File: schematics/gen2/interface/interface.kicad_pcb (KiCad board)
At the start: 2 copper layers, 100 x 91 mm, 17 parts, among them U1 74LS00, U2 74LS00, U4 74LS245, U5 74LS193, U6 74LS193, U7 74LS193, U8 74LS193

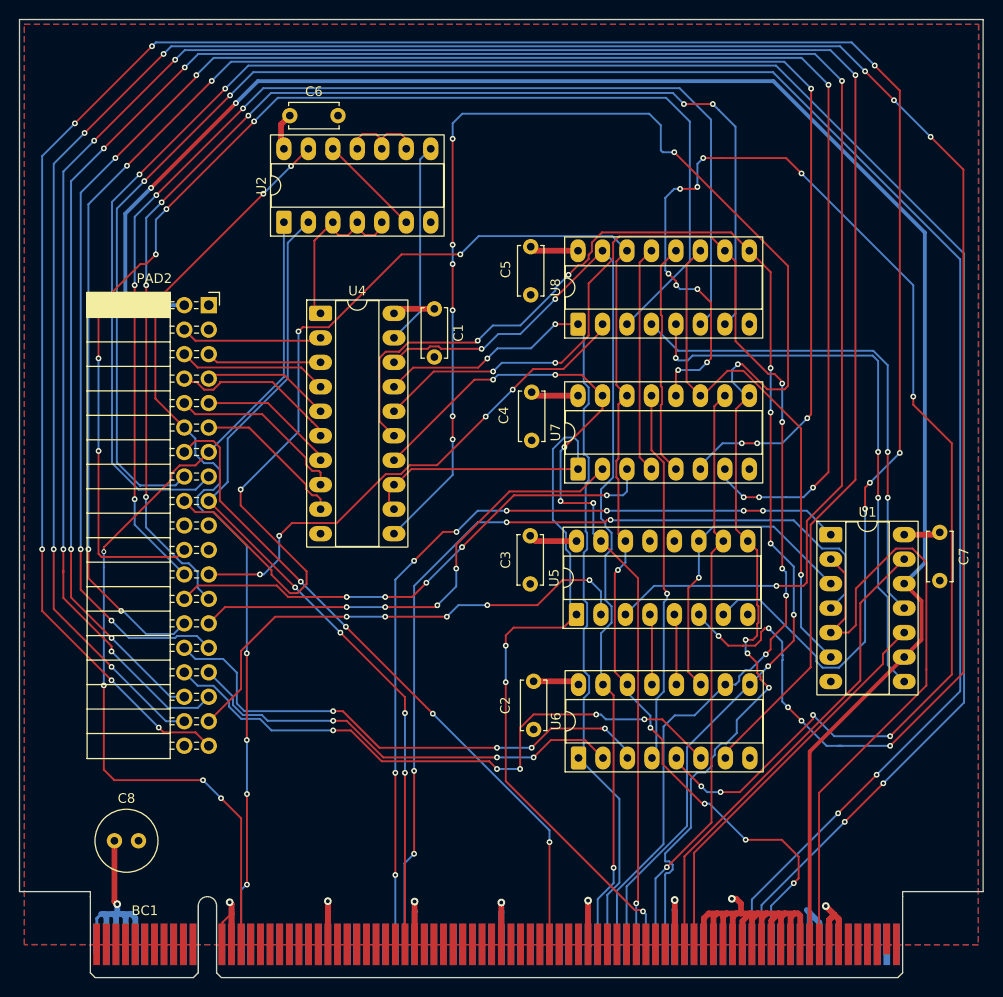
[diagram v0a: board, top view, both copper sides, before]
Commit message: chore(kicad-pcb): added apps ucu logo
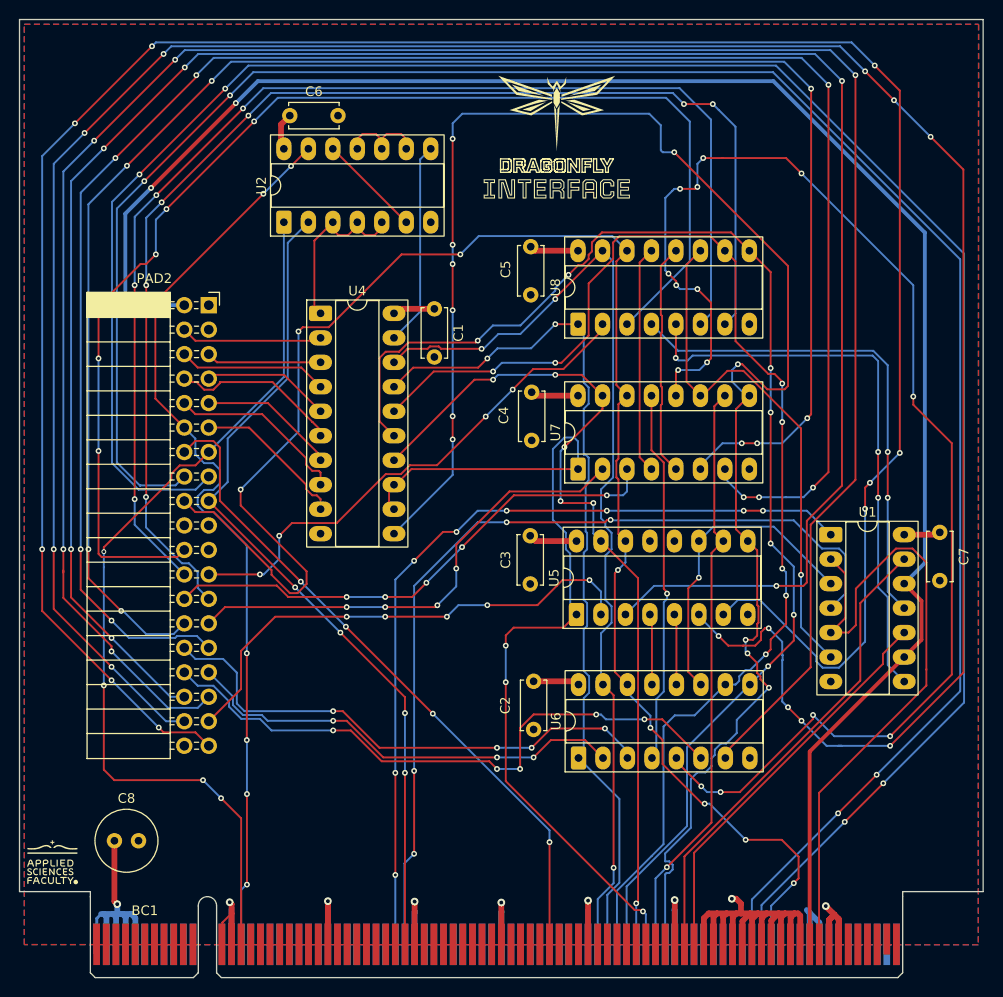
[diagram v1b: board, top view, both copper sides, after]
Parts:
- added kibuzzard-6911D1BC: G***, kibuzzard-6911D1BC, F.Cu at (141.4, 40.2)

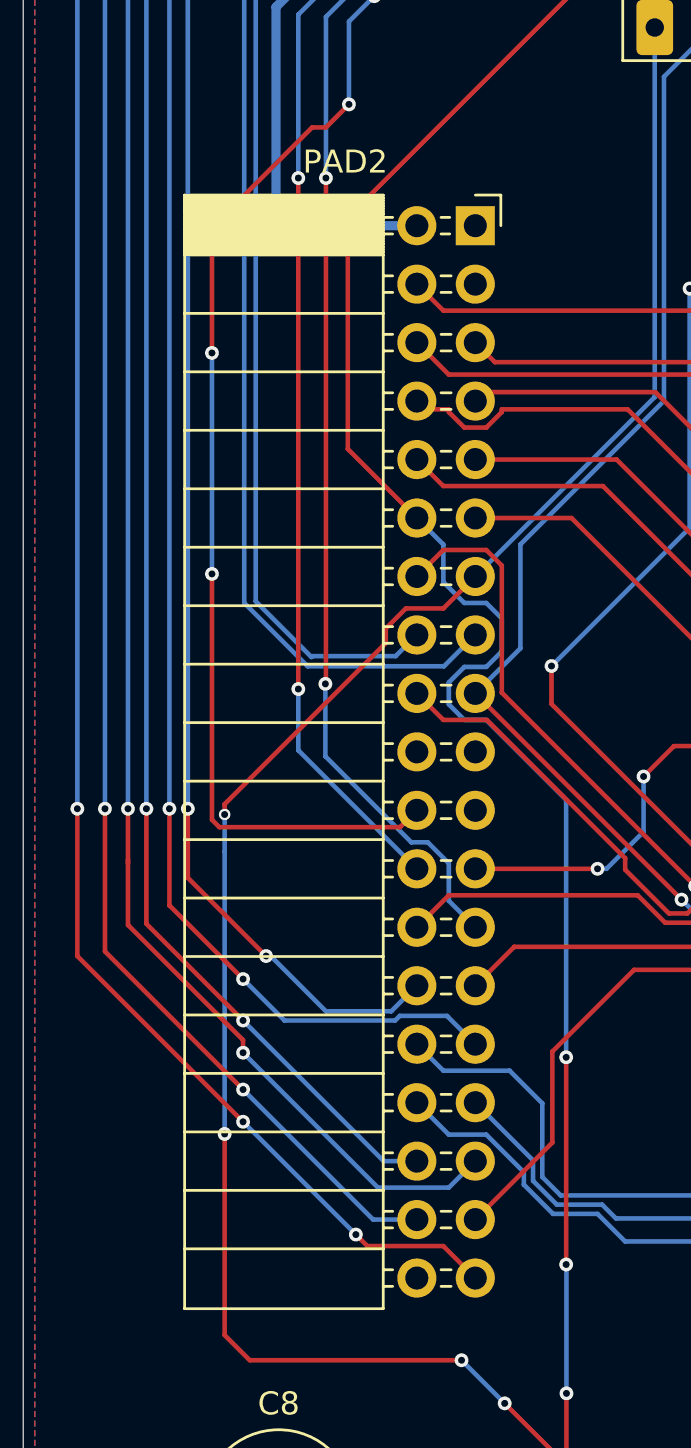
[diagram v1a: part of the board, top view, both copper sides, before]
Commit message: fix(kicad): vcc zones
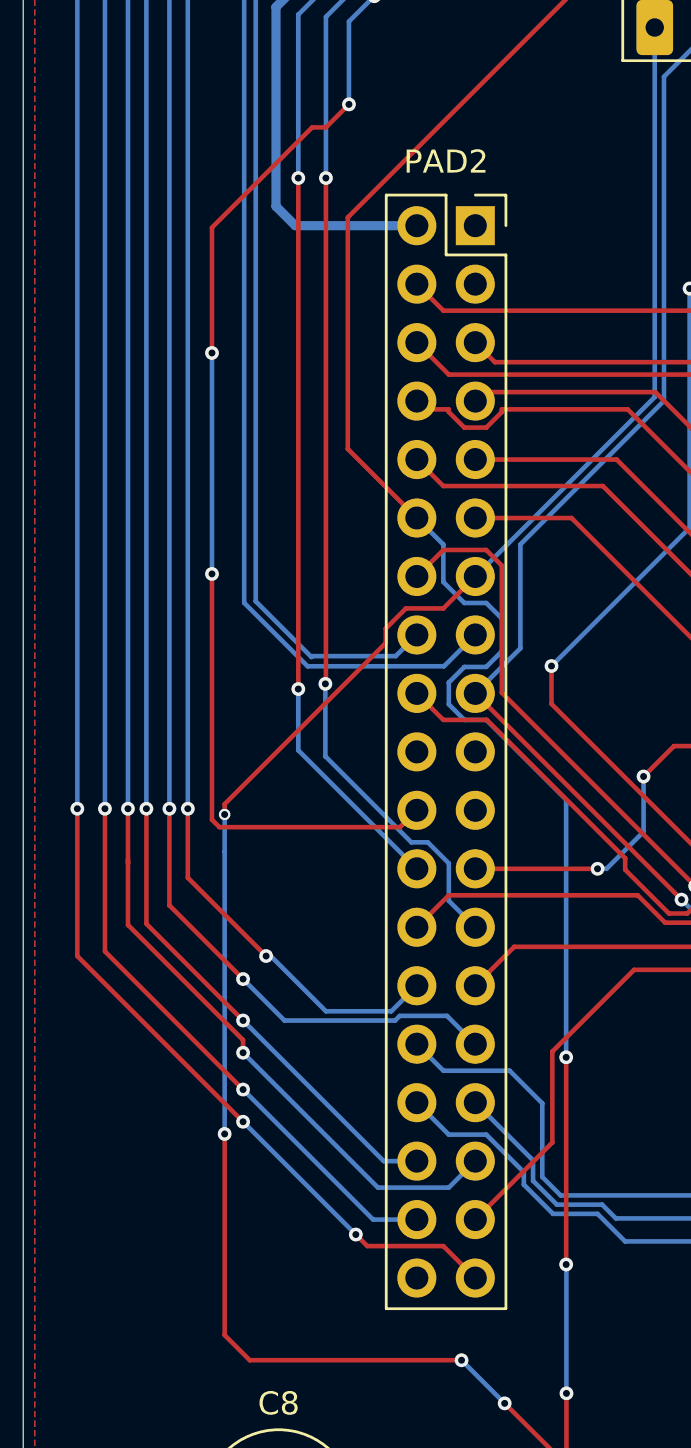
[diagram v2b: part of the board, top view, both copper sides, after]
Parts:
- PAD2: footprint Connector_PinSocket_2.54mm:PinSocket_2x19_P2.54mm_Horizontal -> Connector_PinSocket_2.54mm:PinSocket_2x19_P2.54mm_Vertical
